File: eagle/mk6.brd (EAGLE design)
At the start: 31.3 x 34.7 mm, 13 parts, among them IC2 78L05F, J1 AVR_SPI_PROG_3X2PTH, U1 ATTINY85-20SU

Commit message: v1.4. Added AG-pad, different button than 1.3b
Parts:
- removed S1: SWITCH-MOMENTARY-2TACTILE-SWITCH-SMD-RIGHT-ANGLE, SparkFun-Electromechanical:TACTILE_SWITCH-SMD-RIGHT-ANGLE
- added AG-PAD: JUMPER-SMT_3_1-NC_TRACE_SILK, SparkFun-Jumpers:SMT-JUMPER_3_1-NC_TRACE_SILK
- added S2: K2-1823SA, ube:K2-1823SA
- moved J1 6.60 mm to (28.9, 15.4), turned to 0 degrees
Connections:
- new net SYNCPIN: AG-PAD.2, J1.3, U1.7
- net GND: now also S2.P$2; no longer S1.2
- net H-SYNC: now also AG-PAD.1
- net N$6: now also S2.P$1; no longer S1.1
- net V-SYNC: now also AG-PAD.3; no longer J1.3, U1.7
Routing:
- net SYNCPIN: track 0.00 -> 17.8 mm
- net +5V: track 72.2 -> 61.2 mm, vias 3 -> 2
- net VGREEN: track 34.8 -> 24.5 mm, vias 2 -> 1
- net RST: track 21.9 -> 15.0 mm
- net N$6: track 30.7 -> 24.2 mm
- net H-SYNC: track 13.0 -> 19.4 mm
- net MOSI: track 13.0 -> 8.62 mm
- net GND: track 2.57 -> 0.00 mm, vias 3 -> 4
- net SELECT: track 28.7 -> 26.3 mm
- net PBLUE: track 11.4 -> 9.53 mm
- net PRED: track 13.0 -> 14.4 mm
- net V-SYNC: track 43.1 -> 41.7 mm
- net MONOSIGNAL: track 25.2 -> 24.0 mm
- net VRED: track 28.9 -> 29.9 mm, vias 2 -> 1
- net PGREEN: track 7.98 -> 8.95 mm
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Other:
- board text added: "version 1.4 2020-01-03"
- board text removed: "version 1.3 2018-02-09"

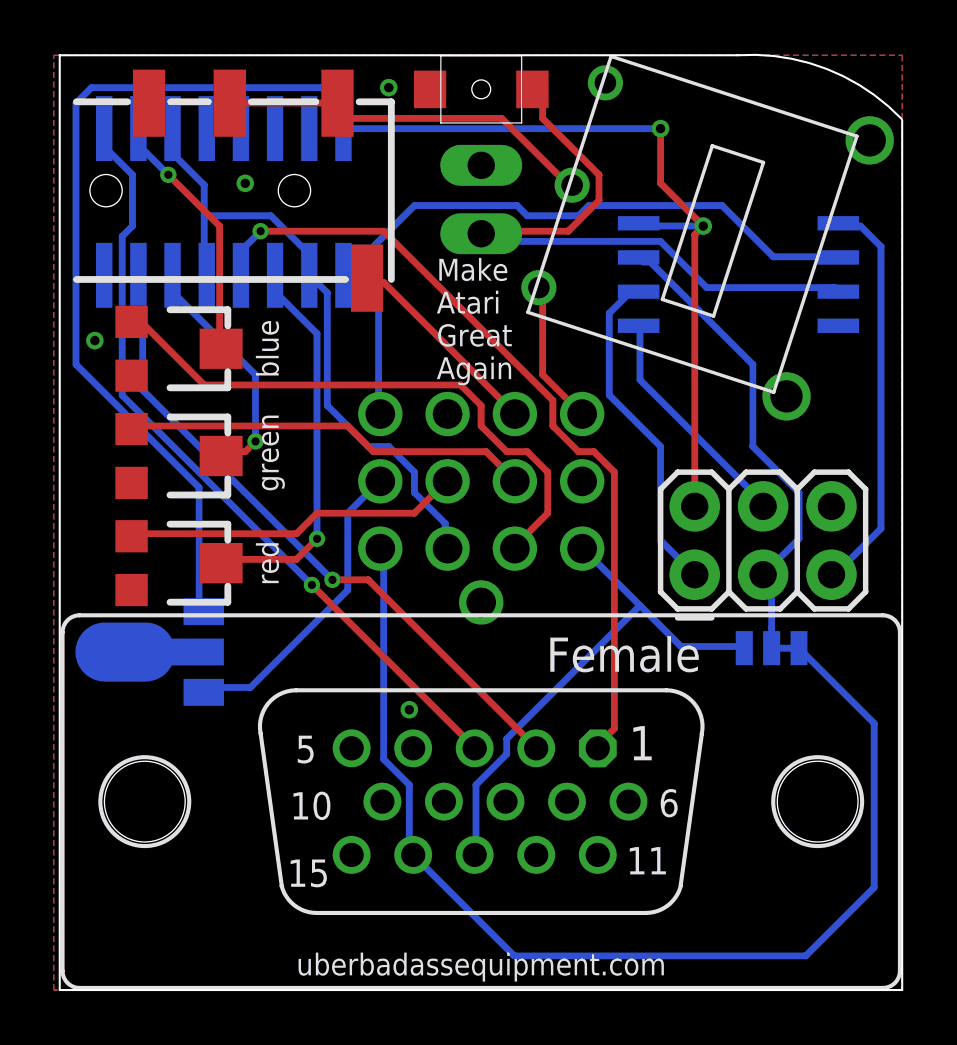
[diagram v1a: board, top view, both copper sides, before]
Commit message: Removed routing since PCB houses differ..
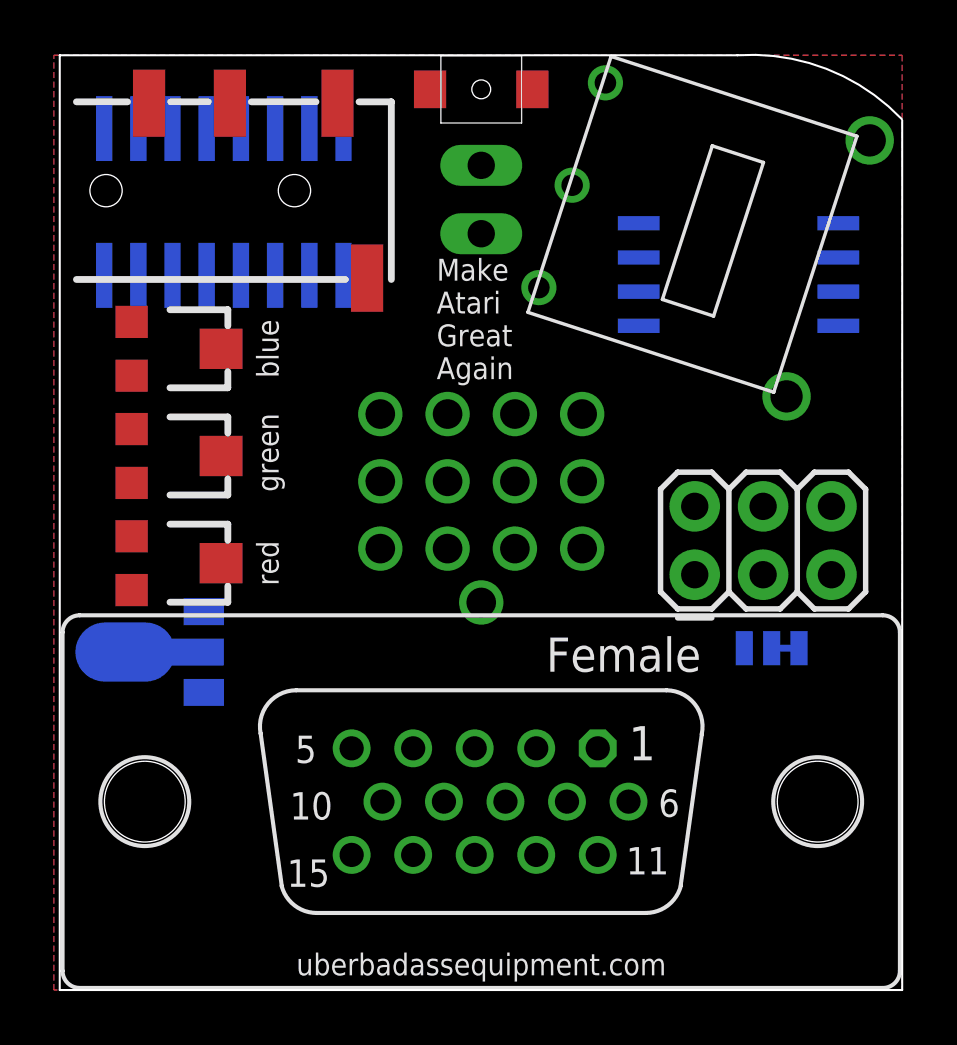
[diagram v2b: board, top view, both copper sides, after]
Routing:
- net +5V: track 61.2 -> 0.00 mm, vias 2 -> 0
- net V-SYNC: track 41.7 -> 0.00 mm
- net VRED: track 29.9 -> 0.00 mm, vias 1 -> 0
- net VBLUE: track 29.1 -> 0.00 mm, vias 1 -> 0
- net SELECT: track 26.3 -> 0.00 mm
- net VGREEN: track 24.5 -> 0.00 mm, vias 1 -> 0
- net N$6: track 24.2 -> 0.00 mm
- net MONOSIGNAL: track 24.0 -> 0.00 mm
- net ABLUE: track 21.6 -> 0.00 mm
- net H-SYNC: track 19.4 -> 0.00 mm
- net SYNCPIN: track 17.8 -> 0.00 mm
- net AGREEN: track 15.2 -> 0.00 mm
- net RST: track 15.0 -> 0.00 mm
- net PRED: track 14.4 -> 0.00 mm, vias 1 -> 0
- net AUDIOPOT: track 14.1 -> 0.00 mm
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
